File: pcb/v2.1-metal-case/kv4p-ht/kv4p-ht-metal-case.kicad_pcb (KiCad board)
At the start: 4 copper layers, 80 x 47 mm, 87 parts, among them J1 Antenna, J5 USB-C Socket, Q1 SS8050, Q2 SS8050, Q3 AO3400A, SW1 Program, SW2 Program, SW3 Reset, SW4 Program, U1 DRA/SA818, U2 AZ1117H-3.3TRG1, U4 CP2102N-A02-GQFN24, U5 ESP32-WROOM-32E-N4

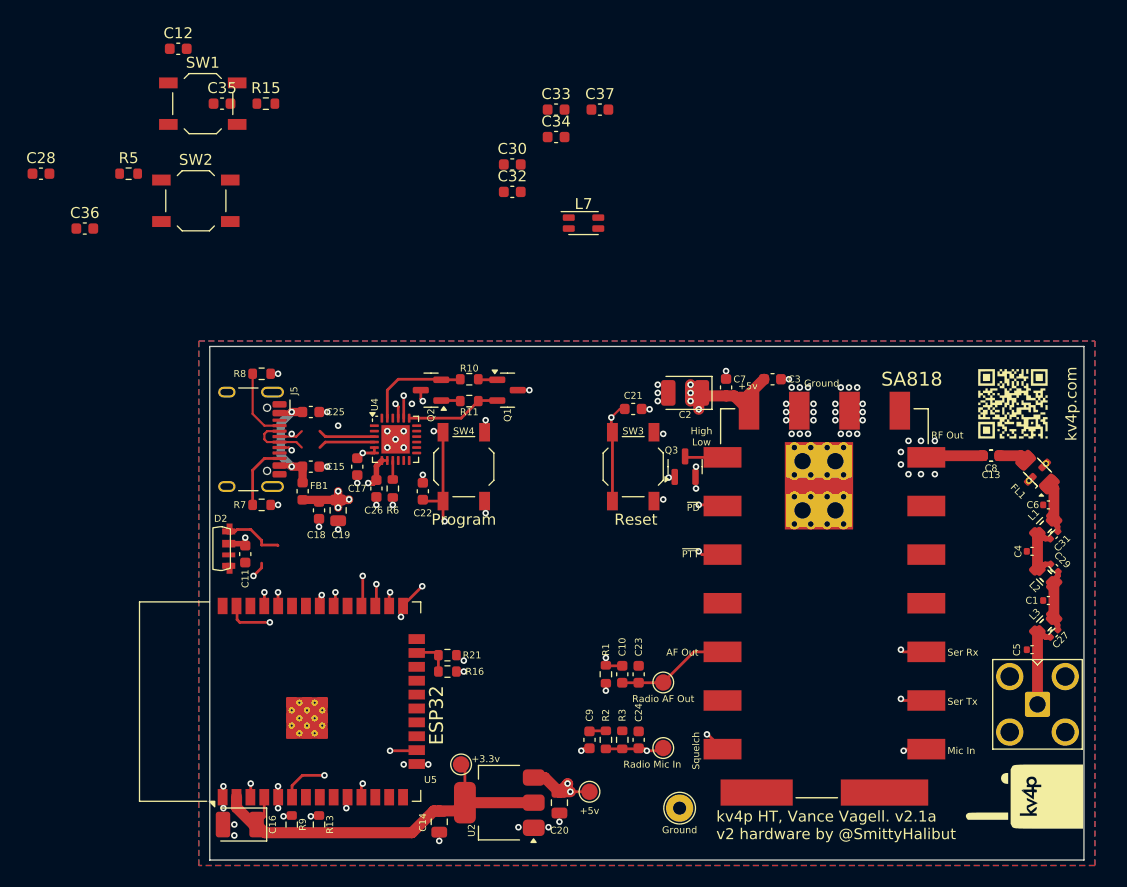
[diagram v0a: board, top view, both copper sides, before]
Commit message: More work on v2.1: UHF support, USB CMCC, 80x50x20mm case. #22
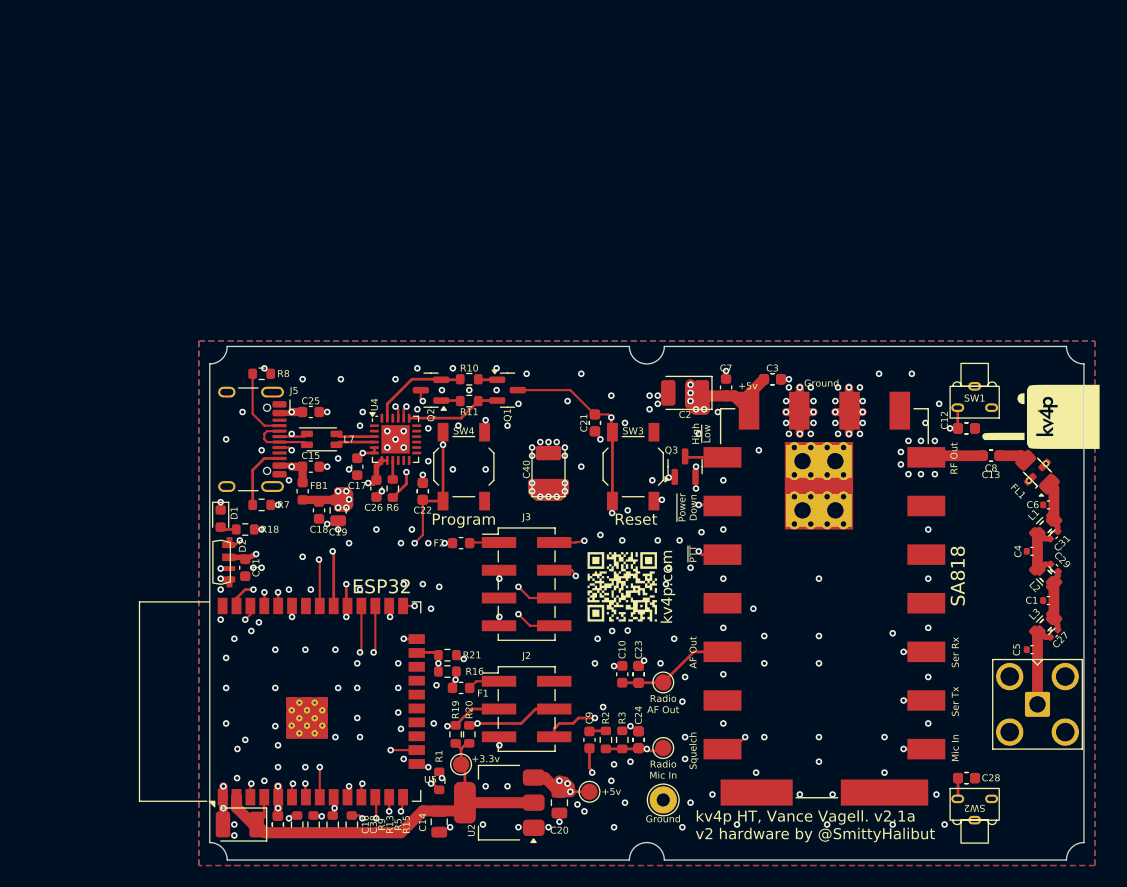
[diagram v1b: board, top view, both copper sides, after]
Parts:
- added C38: 2.2nF Tuned VHF, Capacitor_SMD:C_0603_1608Metric, F.Cu at (196.2, 114.2)
- added C39: 220pF Tune UHF, Capacitor_SMD:C_0603_1608Metric, F.Cu at (196.2, 114.2)
- added C40: 100uF 6.3v, Capacitor_Tantalum_SMD:CP_EIA-3528-21_Kemet-B, F.Cu at (221.0, 81.8)
- added D1: Red, LED_SMD:LED_0603_1608Metric, F.Cu at (191.0, 86.2)
- added F1: 100mA, Fuse:Fuse_0603_1608Metric, F.Cu at (213.0, 101.8)
- added F2: 100mA, Fuse:Fuse_0603_1608Metric, F.Cu at (213.0, 88.5)
- added J2: SAO v.69bis, Connector_PinHeader_2.54mm:PinHeader_2x03_P2.54mm_Vertical_SMD, F.Cu at (219.0, 103.7)
- added J3: GPIO Header, Connector_PinHeader_2.54mm:PinHeader_2x04_P2.54mm_Vertical_SMD, F.Cu at (219.0, 92.2)
- added R18: 1.2k, Resistor_SMD:R_0603_1608Metric, F.Cu at (193.2, 87.2)
- added R19: 1.2k, Resistor_SMD:R_0603_1608Metric, F.Cu at (212.5, 106.0)
- added R20: 1.2k, Resistor_SMD:R_0603_1608Metric, F.Cu at (213.8, 106.0)
- SW1, SW2: value Program -> PTT; footprint Button_Switch_SMD:SW_SPST_TL3342 -> kv4p-ht:SW-Push-SPST-Horizontal-C455252
- moved C28 101.2 mm to (259.2, 110.0)
- moved C36 95.1 mm to (259.2, 110.0), turned to 180 degrees
- moved SW2 91.3 mm to (260.0, 114.2), turned to 180 degrees
- moved C12 80.1 mm to (259.2, 78.0)
- moved SW1 75.1 mm to (260.0, 73.8)
- moved C35 74.3 mm to (259.2, 78.0), turned to 180 degrees
- moved R15 66.4 mm to (203.0, 114.2), turned to 90 degrees
- moved R5 62.4 mm to (201.2, 114.2), turned to 90 degrees
- moved C33 52.2 mm to (229.2, 100.5), turned to -90 degrees
- moved C32 51.5 mm to (229.2, 106.5), turned to -90 degrees
- moved G*** 39.5 mm to (227.8, 92.5)
- moved G*** 34.8 mm to (266.0, 77.0)
- moved C34 34.6 mm to (209.5, 83.8), turned to -90 degrees
- moved L7 31.1 mm to (200.2, 79.0)
- moved C30 30.9 mm to (241.5, 73.5), turned to 180 degrees
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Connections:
- D2 pad 3: unconnected-(D2-DOUT-Pad3) -> /NeoPixel DO
- L7 pad 1: Net-(J5-D--PadA7) -> Net-(J5-D+-PadA6)
- L7 pad 2: Net-(U4-D-) -> Net-(U4-D+)
- L7 pad 3: Net-(U4-D+) -> Net-(U4-D-)
- L7 pad 4: Net-(J5-D+-PadA6) -> Net-(J5-D--PadA7)
- SW1 pad 1: /PTT Button Right -> GND
- SW1 pad 2: GND -> /PTT Button Right
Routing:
- net /PTT Button Right: track 0.00 -> 129.3 mm, vias 0 -> 5
- net /PTT Button Left: track 0.00 -> 64.9 mm, vias 0 -> 1
- net /GPIO35: track 0.00 -> 45.8 mm, vias 0 -> 3
- net /GPIO12: track 0.00 -> 45.6 mm, vias 0 -> 3
- net /SAO SCK: track 0.00 -> 44.0 mm, vias 0 -> 3
- net /GPIO14: track 0.00 -> 42.1 mm, vias 0 -> 3
- net /GPIO27: track 0.00 -> 39.3 mm, vias 0 -> 2
- net /SAO SDA: track 0.00 -> 35.9 mm, vias 0 -> 3
- net +5V: track 30.8 -> 64.5 mm, vias 12 -> 24
- net /GPIO32: track 0.00 -> 33.4 mm, vias 0 -> 3
- net /Stock LED: track 0.00 -> 28.5 mm, vias 0 -> 3
- net /NeoPixel DO: track 0.00 -> 26.7 mm, vias 0 -> 2
- net /ADC Bias: track 29.0 -> 8.55 mm
- net GND: track 0.00 -> 20.1 mm, vias 73 -> 212
- net /GPIO15: track 3.59 -> 21.6 mm, vias 0 -> 3
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- added copper zone on In2.Cu, net +5V
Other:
- outline, holes or cut-outs redrawn
- board text added: "Center scallops are centered."
- board text added: "ESP32 Center"
- board text added: "ESP32 Width"
- board text added: "High ~{Low}"
- board text added: "PTT Buttons"
- board text added: "PTT Buttons, in from edge of board."
- board text added: "RGB LED"
- board text added: "Radio AF Out"
- board text added: "SMA RF Out"
- board text added: "Total Length"
- board text added: "Total Width"
- board text added: "USB-C"
- board text added: "~{Power} Down"
- board text removed: "High Low"
- board text removed: "Pwr LED"
- board text removed: "Right Button"
- board text removed: "~{PD}"

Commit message: v2.1b as ordered 2025-04-17. VHF and UHF #22. SAO headers. PTT buttons. User LED.
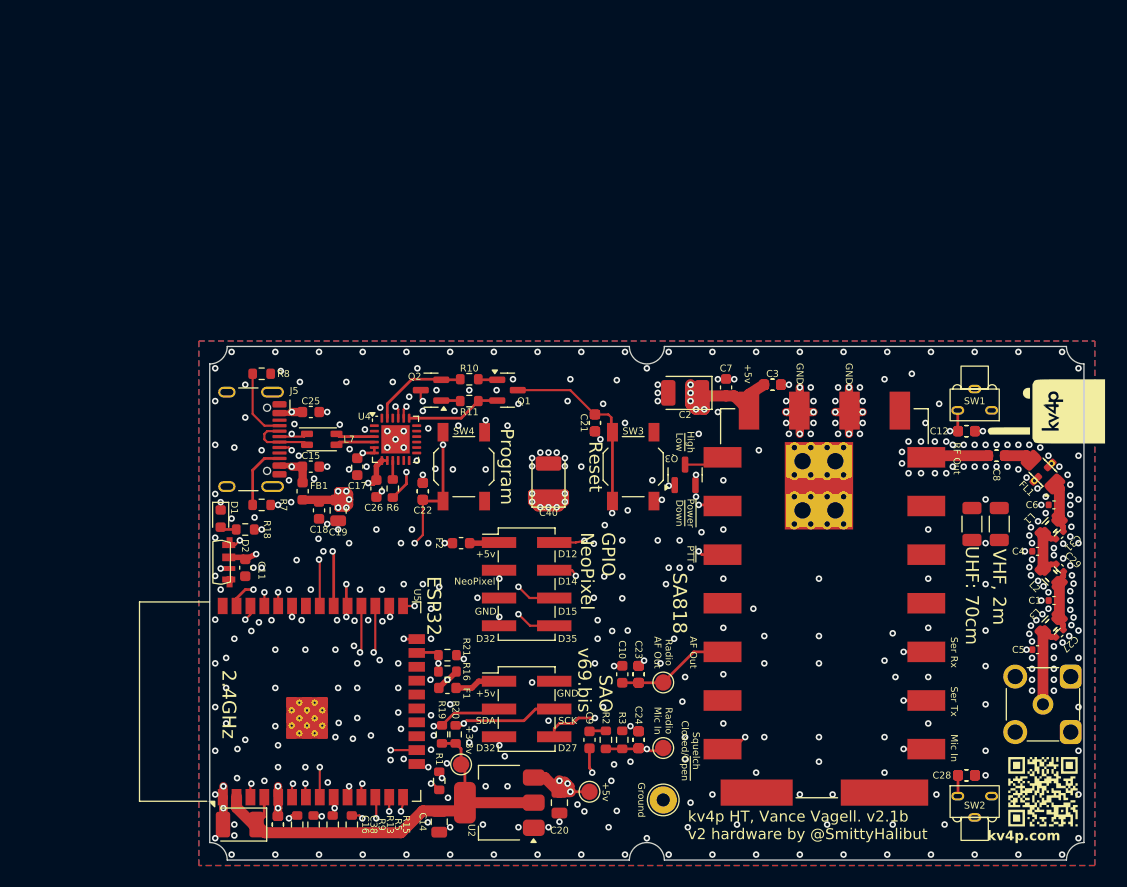
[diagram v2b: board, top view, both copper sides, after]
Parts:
- added R22: VHF, Resistor_SMD:R_1206_3216Metric, F.Cu at (262.2, 86.8)
- added R23: UHF, Resistor_SMD:R_1206_3216Metric, F.Cu at (259.8, 86.8)
- J1: footprint Connector_Coaxial:SMA_Amphenol_901-143_Horizontal -> Libraries:Conn_SMA_Close-to-board-edge
- moved G*** 42.8 mm to (266.2, 111.2)
- moved F1 1.25 mm to (211.8, 101.8)
- moved R19 1.25 mm to (211.2, 106.0)
- moved R20 1.25 mm to (212.5, 106.0)
- moved C40 0.96 mm to (221.0, 82.8)
- moved Q3 0.75 mm to (233.5, 82.2)
- moved G*** 0.71 mm to (266.5, 76.5)
- moved C1 0.50 mm to (267.2, 93.8)
- moved C13 0.50 mm to (262.0, 80.5)
- moved C27 0.50 mm to (267.8, 96.8)
- moved C29 0.50 mm to (267.8, 90.8)
- moved C3 0.50 mm to (241.5, 74.0)
- moved C30 0.50 mm to (241.5, 74.0)
- moved C31 0.50 mm to (267.8, 87.8)
- moved C4 0.50 mm to (265.8, 89.2)
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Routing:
- net /PTT Button Right: track 129.3 -> 126.1 mm
- net Net-(J2-Pin_1): track 2.94 -> 4.19 mm
- net Net-(Q3-G): track 51.0 -> 50.2 mm
- net +5V: track 64.5 -> 65.3 mm
- net Net-(U1-ANT): track 5.21 -> 5.71 mm
- net /Enable/~{Reset}: track 84.6 -> 84.7 mm, vias 6 -> 5
- net GND: vias 212 -> 405
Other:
- board text added: "2.4GHz"
- board text added: "All pins, on both headers are 0.1{dblquote} spaced"
- board text added: "All scallops, r=1.6mm, for M3 screws"
- board text added: "Buttons"
- board text added: "Center line"
- board text added: "Center of 8 pin header"
- board text added: "Center of both headers"
- board text added: "D12"
- board text added: "D14"
- board text added: "D15"
- board text added: "D27"
- board text added: "D32"
- board text added: "D35"
- board text added: "GND"
- board text added: "GPIO NeoPixel"
- board text added: "NeoPixel"
- board text added: "PTT button surface in from edge of board."
- board text added: "Pin headers are 0.1{dblquote} spaced, including betwteen headers. They are anchored to the mm grid at center of 8 pin header."
- board text added: "Program button"
- board text added: "Reset button"
- board text added: "SAO v69.bis"
- board text added: "SCK"
- board text added: "SDA"
- board text added: "Squelch Closed/~{Open}"
- board text added: "UHF: 70cm"
- board text added: "VHF, 2m"
- board text added: "kv4p HT, Vance Vagell. v2.1b v2 hardware by @SmittyHalibut"
- board text added: "~{Power} ~{Down}"
- board text removed: "PTT Buttons, in from edge of board."
- board text removed: "Squelch"
- board text removed: "kv4p HT, Vance Vagell. v2.1a v2 hardware by @SmittyHalibut"
- board text removed: "~{Power} Down"
